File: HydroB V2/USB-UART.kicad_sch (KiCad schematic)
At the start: 5 parts, among them J26 USB_C_2.0, SW3 K2, SW4 K1

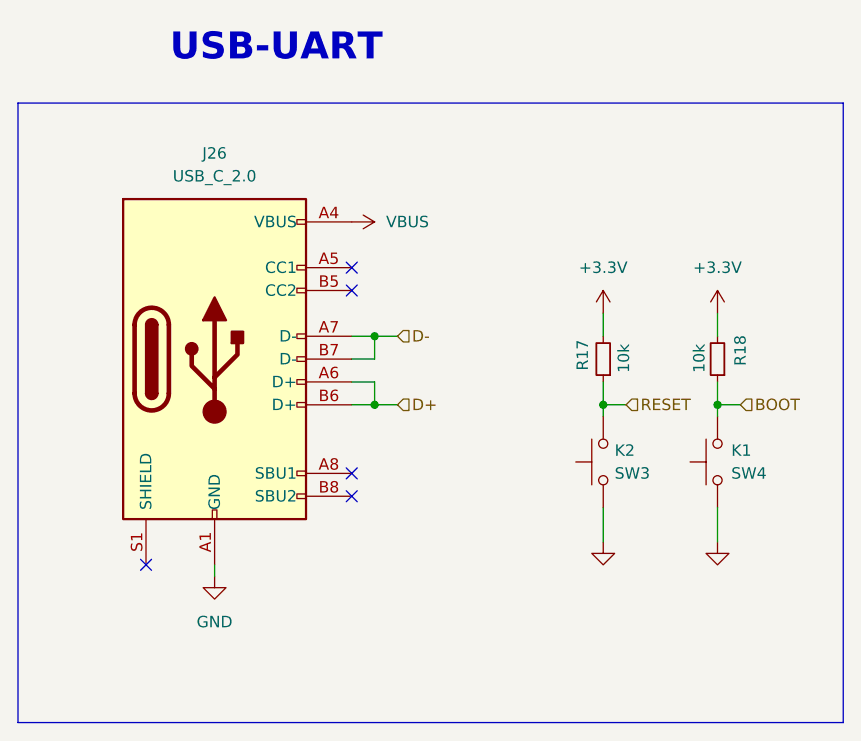
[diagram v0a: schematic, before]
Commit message: Update power supply and connector of sensor
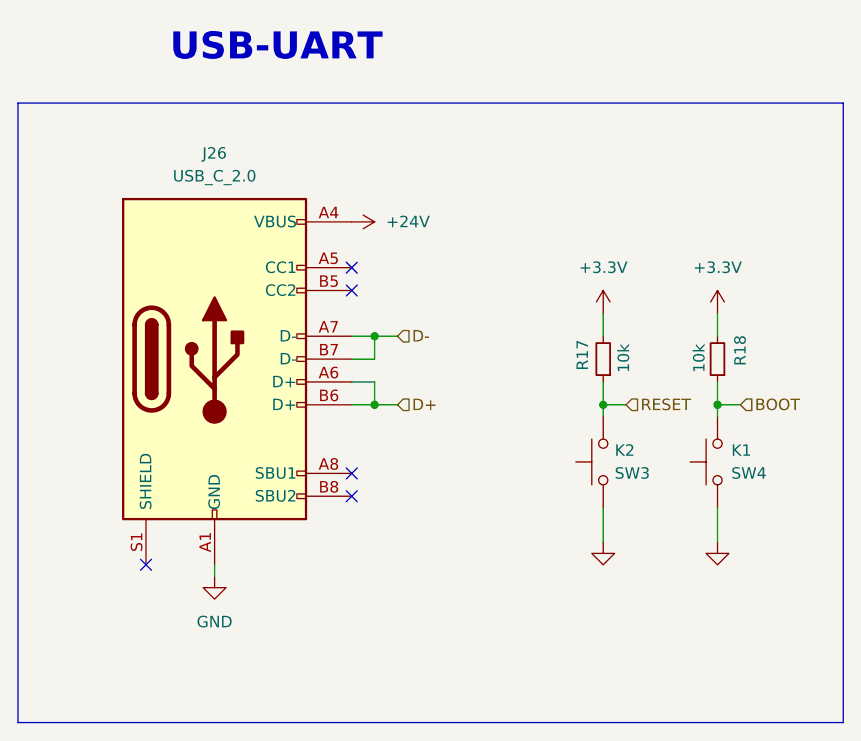
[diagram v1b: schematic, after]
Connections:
- net VBUS renamed +24V
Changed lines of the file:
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@@
+	)
+	(symbol
+		(lib_id "power:+24V")
+		(at 140.97 80.01 270)
+		(unit 1)
+		(exclude_from_sim no)
+		(in_bom yes)
+		(on_board yes)
+		(dnp no)
+		(fields_autoplaced yes)
+		(property "Reference" "#PWR026"
+			(at 137.16 80.01 0)
+			(effects
+				(font
+					(size 1.27 1.27)
+				)
+				(hide yes)
+			)
+		)
+		(property "Value" "+24V"
+			(at 144.78 80.0099 90)
+			(effects
+				(font
+					(size 1.27 1.27)
+				)
+				(justify left)
+			)
+		)
+		(property "Footprint" ""
+			(at 140.97 80.01 0)
+			(effects
+				(font
+					(size 1.27 1.27)
+				)
+				(hide yes)
+			)
+		)
+		(property "Datasheet" ""
+			(at 140.97 80.01 0)
+			(effects
+				(font
+					(size 1.27 1.27)
+				)
+				(hide yes)
+			)
+		)
+		(property "Description" "Power symbol creates a global label with name \"+24V\""
+			(at 140.97 80.01 0)
+			(effects
+				(font
+					(size 1.27 1.27)
+				)
+				(hide yes)
+			)
+		)
+		(pin "1"
+		)
+		(instances
+			(project "HydroB V2"
+				(path "/0a8bb8df-6bdd-4d10-933b-144d3fa4f517/b5cea501-254b-4c6a-af47-d8c013c279ab/768fe99b-0ade-4ebe-9148-804d23124789"
+					(reference "#PWR026")
+					(unit 1)
+				)
+			)
+		)
 	)
 	(symbol
@@
 					(unit 1)
 				)
-			)
-		)
-	)
-	(symbol
-		(lib_id "power:VBUS")
-		(at 140.97 80.01 270)
-		(unit 1)
-		(exclude_from_sim no)
-		(in_bom yes)
-		(on_board yes)
-		(dnp no)
-		(fields_autoplaced yes)
-		(property "Reference" "#PWR090"
-			(at 137.16 80.01 0)
-			(effects
-				(font
-					(size 1.27 1.27)
-				)
-				(hide yes)
-			)
-		)
-		(property "Value" "VBUS"
-			(at 144.78 80.0099 90)
-			(effects
-				(font
-					(size 1.27 1.27)
-				)
-				(justify left)
-			)
-		)
-		(property "Footprint" ""
-			(at 140.97 80.01 0)
-			(effects
-				(font
-					(size 1.27 1.27)
-				)
-				(hide yes)
-			)
-		)
-		(property "Datasheet" ""
-			(at 140.97 80.01 0)
-			(effects
-				(font
-					(size 1.27 1.27)
-				)
-				(hide yes)
-			)
-		)
-		(property "Description" "Power symbol creates a global label with name \"VBUS\""
-			(at 140.97 80.01 0)
-			(effects
-				(font
-					(size 1.27 1.27)
-				)
-				(hide yes)
-			)
-		)
-		(pin "1"
-		)
-		(instances
-			(project "HydroB V2"
-				(path "/0a8bb8df-6bdd-4d10-933b-144d3fa4f517/b5cea501-254b-4c6a-af47-d8c013c279ab/768fe99b-0ade-4ebe-9148-804d23124789"
-					(reference "#PWR090")
-					(unit 1)
-				)
